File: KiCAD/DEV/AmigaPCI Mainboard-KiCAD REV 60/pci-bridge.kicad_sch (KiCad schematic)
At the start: 43 parts, among them CN109 SPI, CN110 SPI, U109 ICE40HX4K-TQ144, U109F1 W25X20CLSN, U110 ICE40HX4K-TQ144, U110F1 W25X20CLSN

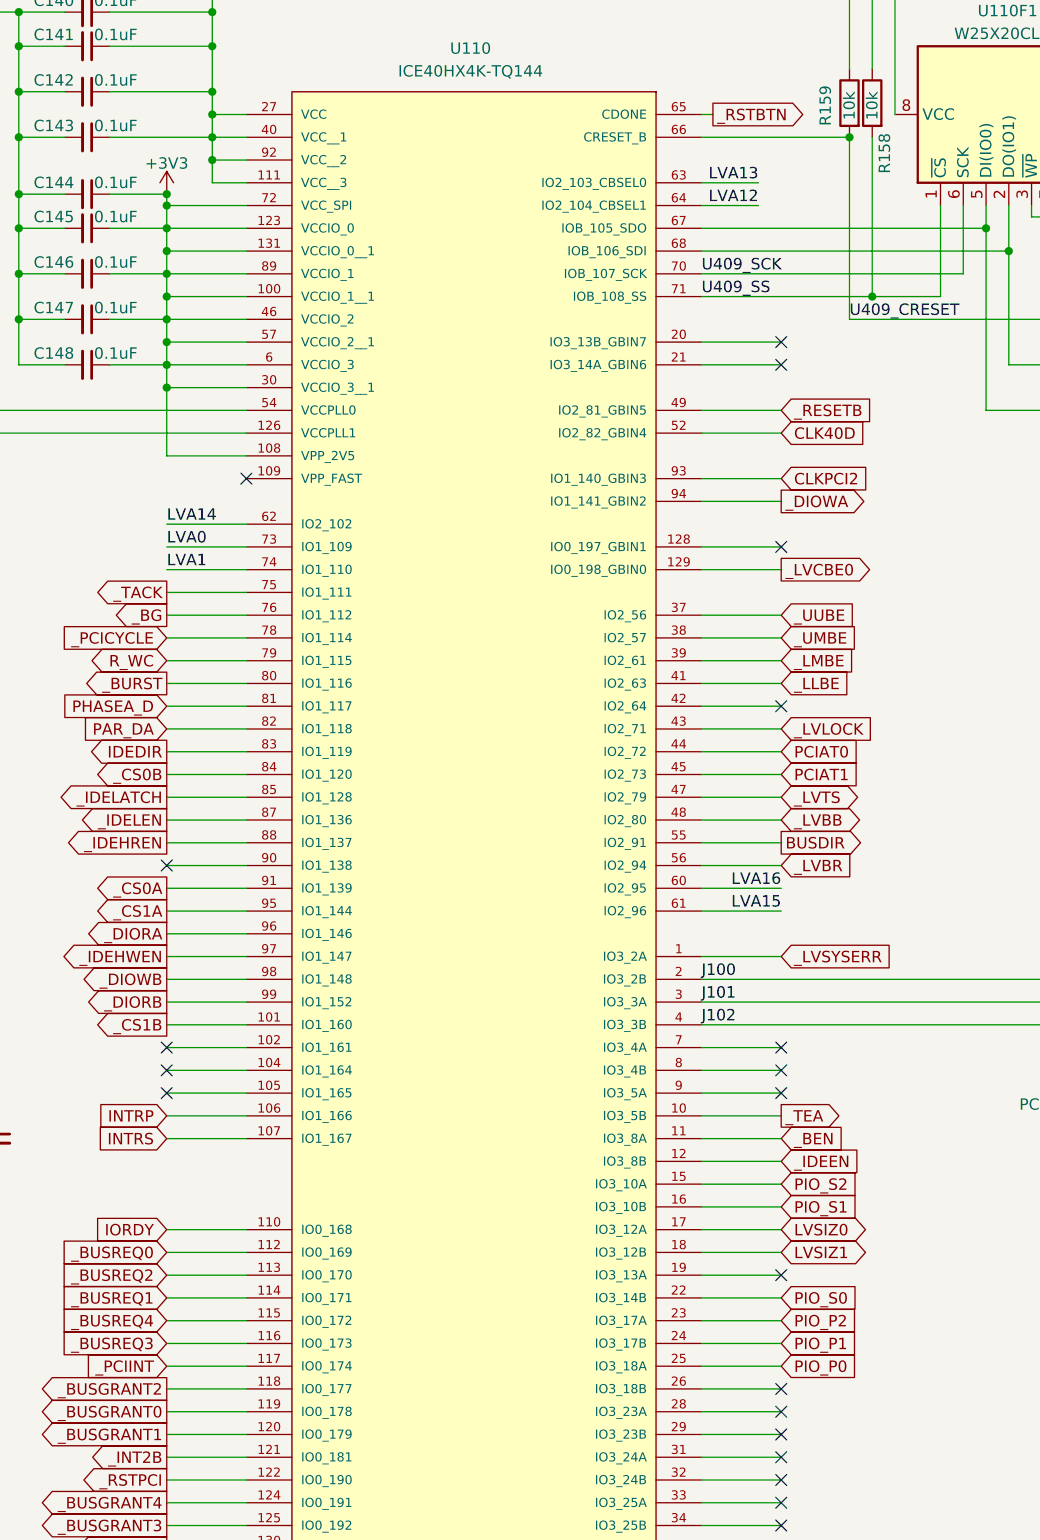
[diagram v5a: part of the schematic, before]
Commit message: Add flash and remove HID buffer.
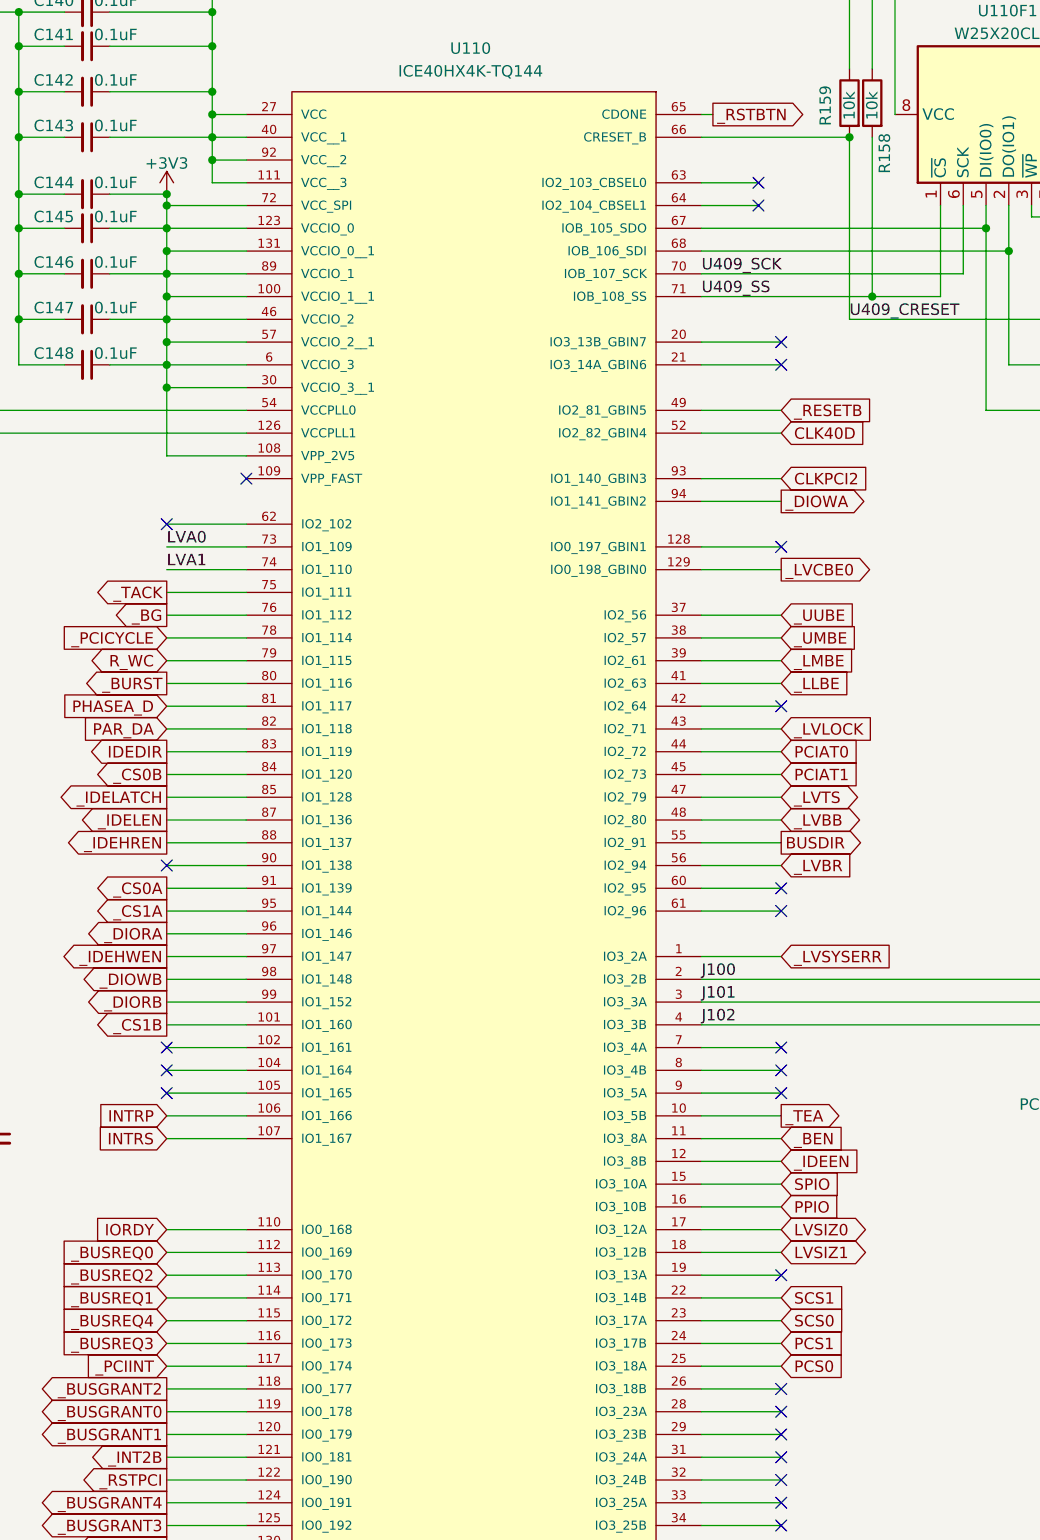
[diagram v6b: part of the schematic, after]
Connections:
- net LVA12: no longer U110.64 (IO2_104_CBSEL1)
- net LVA13: no longer U110.63 (IO2_103_CBSEL0)
- net LVA14: no longer U110.62 (IO2_102)
- net LVA15: no longer U110.61 (IO2_96)
- net LVA16: no longer U110.60 (IO2_95)
- net PIO_P0 renamed PCS0
- net PIO_P1 renamed PCS1
- net PIO_P2 renamed SCS0
- net PIO_S0 renamed SCS1
- net PIO_S1 renamed PPIO
- net PIO_S2 renamed SPIO
- no-connect marks 38 -> 43
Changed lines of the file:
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@@
 	(title_block
 		(title "AMIGA PCI")
-		(date "2025-05-27")
+		(date "2025-06-26")
 		(rev "6.0")
 	)
@@
 	)
 	(no_connect
+		(at 281.94 147.32)
+	)
+	(no_connect
 		(at 281.94 203.2)
 	)
@@
 	)
 	(no_connect
+		(at 279.4 66.04)
+	)
+	(no_connect
 		(at 281.94 106.68)
 	)
@@
 	)
 	(no_connect
+		(at 213.36 104.14)
+	)
+	(no_connect
+		(at 281.94 144.78)
+	)
+	(no_connect
 		(at 123.19 133.35)
 	)
@@
 	)
 	(no_connect
+		(at 279.4 68.58)
+	)
+	(no_connect
 		(at 213.36 167.64)
 	)
@@
 		)
 	)
-	(label "LVA12"
-		(at 279.4 68.58 180)
-		(effects
-			(font
-				(size 1.27 1.27)
-			)
-			(justify right bottom)
-		)
-	)
 	(label "LVD25"
 		(at 383.54 175.26 0)
@@
 		)
 	)
-	(label "LVA15"
-		(at 281.94 147.32 180)
-		(effects
-			(font
-				(size 1.27 1.27)
-			)
-			(justify right bottom)
-		)
-	)
 	(label "LVAD6"
 		(at 342.9 88.9 0)
@@
 		)
 	)
-	(label "LVA14"
-		(at 213.36 104.14 0)
-		(effects
-			(font
-				(size 1.27 1.27)
-			)
-			(justify left bottom)
-		)
-	)
 	(label "LVA26"
 		(at 363.22 170.18 0)
@@
 		)
 	)
-	(label "LVA13"
-		(at 279.4 66.04 180)
-		(effects
-			(font
-				(size 1.27 1.27)
-			)
-			(justify right bottom)
-		)
-	)
 	(label "U409_SDI"
 		(at 314.96 91.44 0)
@@
 		)
 	)
-	(label "LVA16"
-		(at 281.94 144.78 180)
-		(effects
-			(font
-				(size 1.27 1.27)
-			)
-			(justify right bottom)
-		)
-	)
 	(label "LVD27"
 		(at 383.54 182.88 0)
@@
 		)
 	)
-	(global_label "PIO_S0"
+	(global_label "SCS1"
 		(shape input)
 		(at 281.94 190.5 0)
@@
 		)
 	)
-	(global_label "PIO_P1"
+	(global_label "PCS1"
 		(shape input)
 		(at 281.94 195.58 0)
@@
 		)
 	)
-	(global_label "PIO_S1"
+	(global_label "PPIO"
 		(shape input)
 		(at 281.94 180.34 0)
@@
 		)
 	)
-	(global_label "PIO_S2"
+	(global_label "SPIO"
 		(shape input)
 		(at 281.94 177.8 0)
@@
 		)
 	)
-	(global_label "PIO_P0"
+	(global_label "PCS0"
 		(shape input)
 		(at 281.94 198.12 0)
@@
 		)
 	)
-	(global_label "PIO_P2"
+	(global_label "SCS0"
 		(shape input)
 		(at 281.94 193.04 0)
